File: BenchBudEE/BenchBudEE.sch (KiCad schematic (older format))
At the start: 0 parts

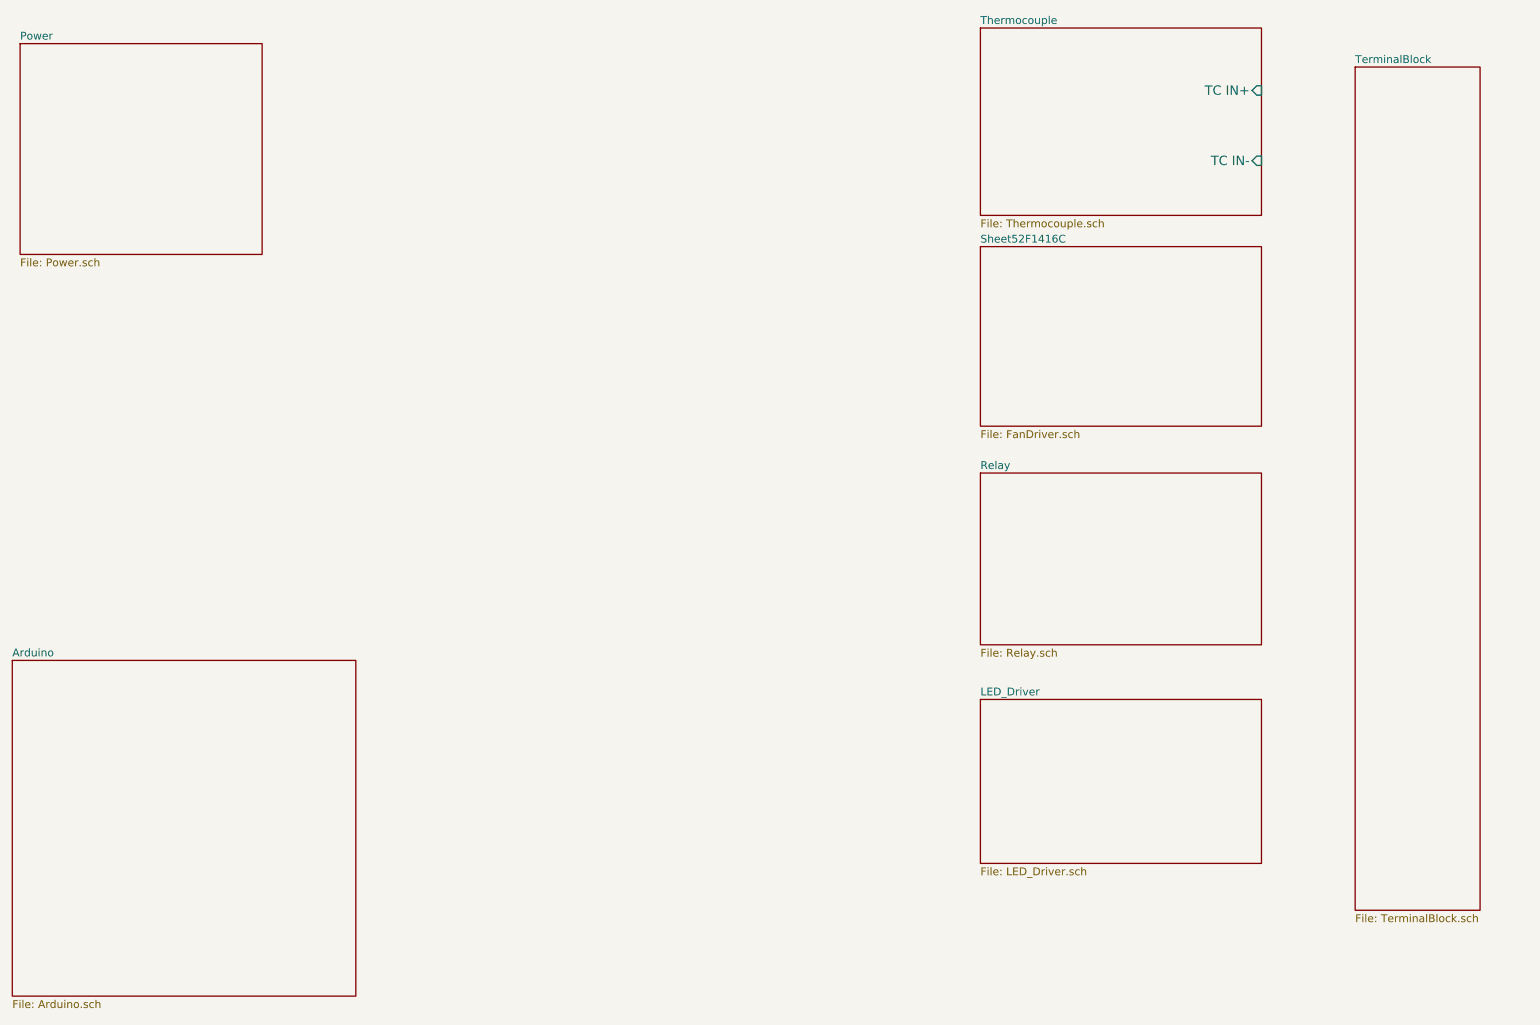
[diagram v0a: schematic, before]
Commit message: Added initial module I/O
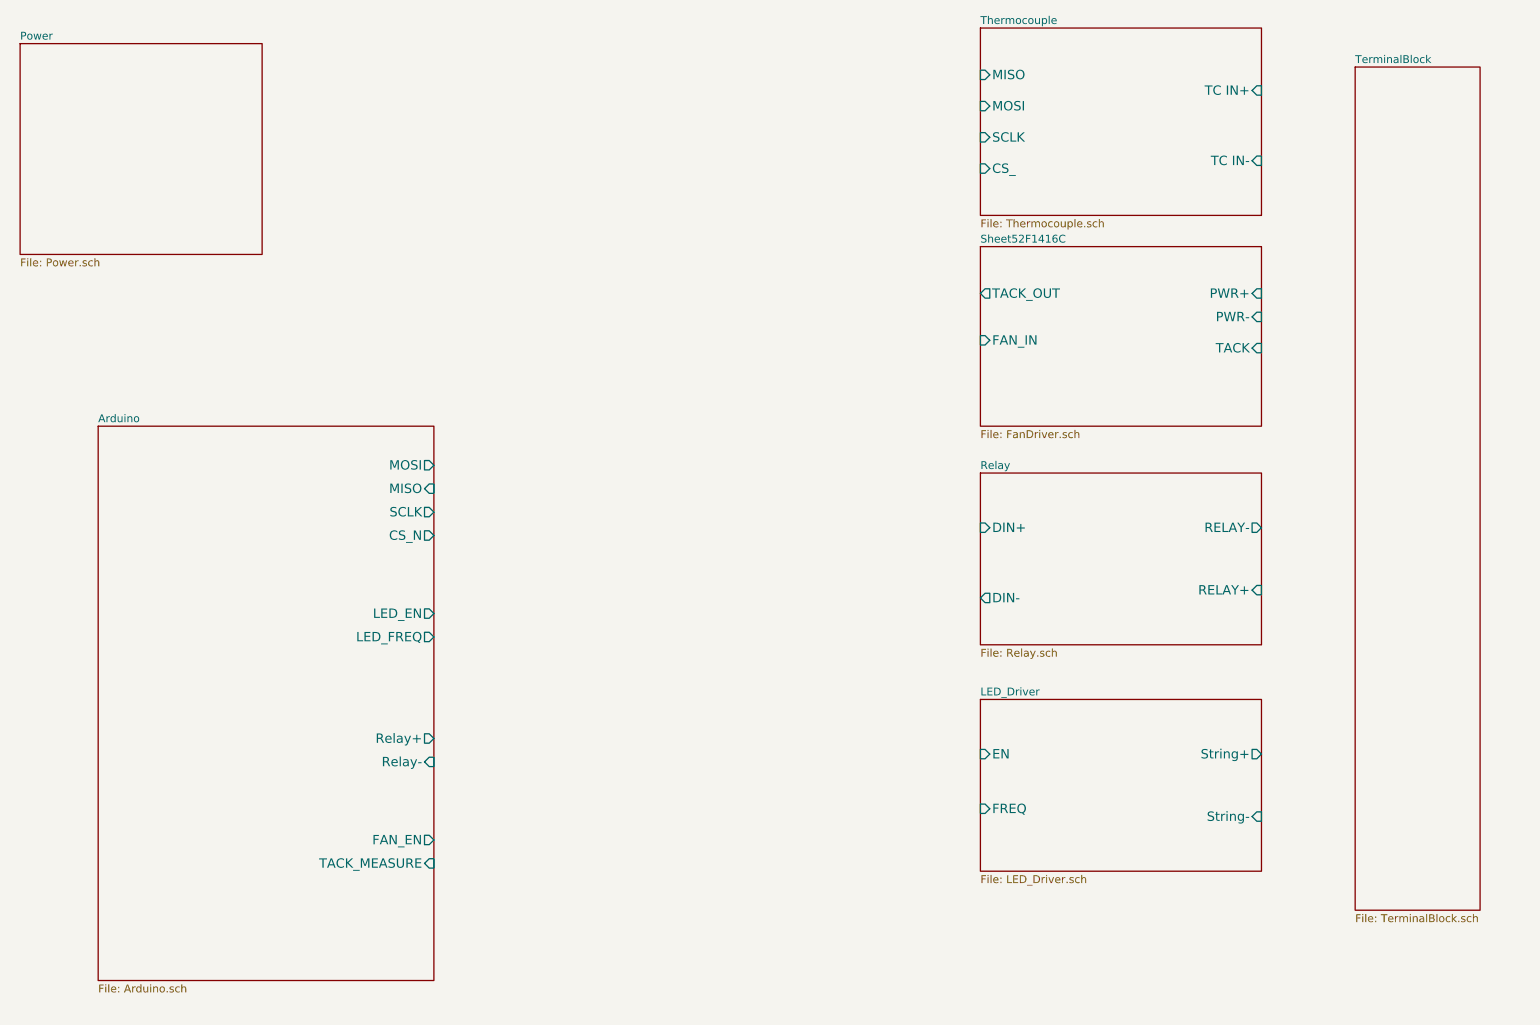
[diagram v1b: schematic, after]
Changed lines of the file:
@@
 F2 "TC IN+" I R 9200 1450 60
 F3 "TC IN-" I R 9200 1900 60
+F4 "MISO" I L 7400 1350 60
+F5 "MOSI" I L 7400 1550 60
+F6 "SCLK" I L 7400 1750 60
+F7 "CS_" I L 7400 1950 60
 $EndSheet
 $Sheet
@@
 F0 "Sheet52F1416C" 50
 F1 "FanDriver.sch" 50
+F2 "PWR+" I R 9200 2750 60
+F3 "PWR-" I R 9200 2900 60
+F4 "TACK" I R 9200 3100 60
+F5 "TACK_OUT" O L 7400 2750 60
+F6 "FAN_IN" I L 7400 3050 60
 $EndSheet
 $Sheet
-S 1200 5100 2200 2150
+S 1750 3600 2150 3550
 U 52F141E3
 F0 "Arduino" 50
 F1 "Arduino.sch" 50
+F2 "MOSI" O R 3900 3850 60
+F3 "MISO" I R 3900 4000 60
+F4 "SCLK" O R 3900 4150 60
+F5 "CS_N" O R 3900 4300 60
+F6 "Relay+" O R 3900 5600 60
+F7 "Relay-" I R 3900 5750 60
+F8 "LED_EN" O R 3900 4800 60
+F9 "LED_FREQ" O R 3900 4950 60
+F10 "FAN_EN" O R 3900 6250 60
+F11 "TACK_MEASURE" I R 3900 6400 60
 $EndSheet
 $Sheet
@@
 F0 "Relay" 50
 F1 "Relay.sch" 50
+F2 "DIN+" I L 7400 4250 60
+F3 "DIN-" O L 7400 4700 60
+F4 "RELAY-" O R 9200 4250 60
+F5 "RELAY+" I R 9200 4650 60
 $EndSheet
 $Sheet
-S 7400 5350 1800 1050
+S 7400 5350 1800 1100
 U 52F14293
 F0 "LED_Driver" 50
 F1 "LED_Driver.sch" 50
+F2 "EN" I L 7400 5700 60
+F3 "FREQ" I L 7400 6050 60
+F4 "String+" O R 9200 5700 60
+F5 "String-" I R 9200 6100 60
 $EndSheet
 $Sheet

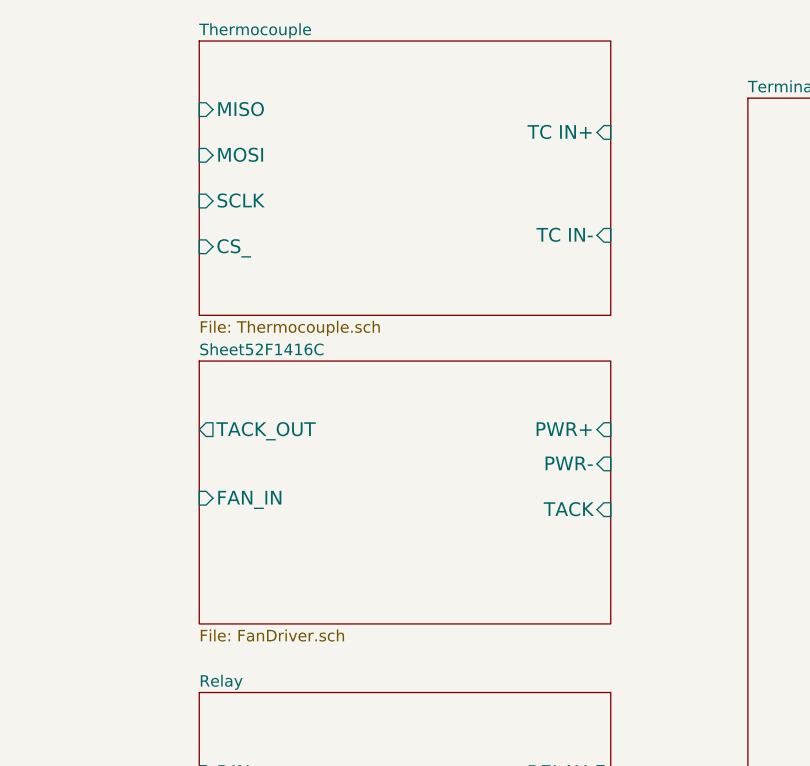
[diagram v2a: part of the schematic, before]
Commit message: Created Fan Module block diagram + added new I/O + minor spelling corrections
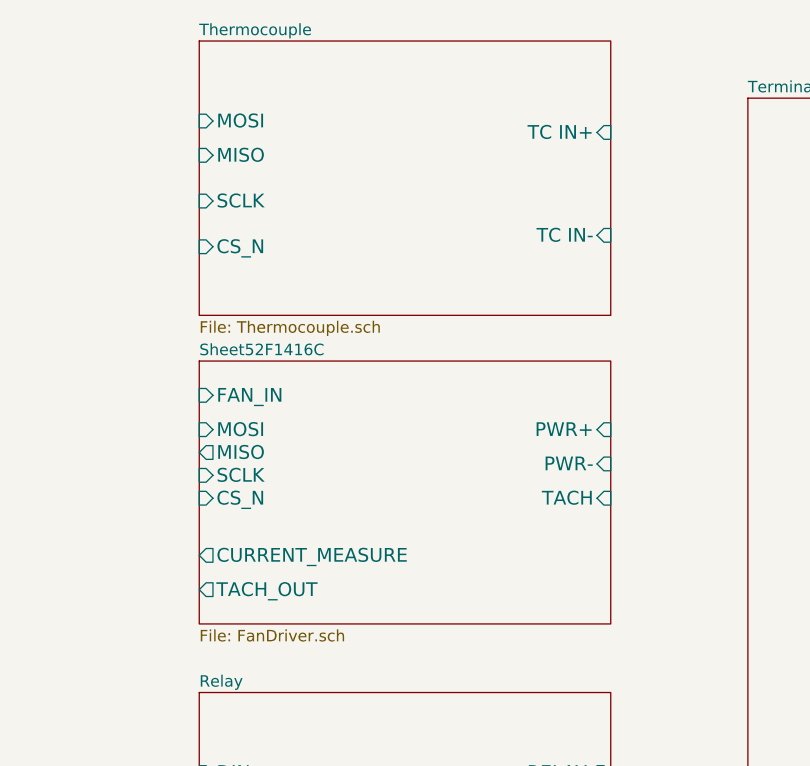
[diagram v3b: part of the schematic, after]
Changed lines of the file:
@@
 $EndDescr
-$Sheet
-S 7400 1050 1800 1200
-U 52F14139
-F0 "Thermocouple" 50
-F1 "Thermocouple.sch" 50
-F2 "TC IN+" I R 9200 1450 60
-F3 "TC IN-" I R 9200 1900 60
-F4 "MISO" I L 7400 1350 60
-F5 "MOSI" I L 7400 1550 60
-F6 "SCLK" I L 7400 1750 60
-F7 "CS_" I L 7400 1950 60
-$EndSheet
-$Sheet
-S 7400 2450 1800 1150
-U 52F1416D
-F0 "Sheet52F1416C" 50
-F1 "FanDriver.sch" 50
-F2 "PWR+" I R 9200 2750 60
-F3 "PWR-" I R 9200 2900 60
-F4 "TACK" I R 9200 3100 60
-F5 "TACK_OUT" O L 7400 2750 60
-F6 "FAN_IN" I L 7400 3050 60
-$EndSheet
 $Sheet
 S 1750 3600 2150 3550
@@
 F1 "Power.sch" 50
 $EndSheet
+$Sheet
+S 7400 2450 1800 1150
+U 52F1416D
+F0 "Sheet52F1416C" 50
+F1 "FanDriver.sch" 50
+F2 "PWR+" I R 9200 2750 60
+F3 "PWR-" I R 9200 2900 60
+F4 "FAN_IN" I L 7400 2600 60
+F5 "TACH" I R 9200 3050 60
+F6 "TACH_OUT" O L 7400 3450 60
+F7 "CURRENT_MEASURE" O L 7400 3300 60
+F8 "MOSI" I L 7400 2750 60
+F9 "MISO" O L 7400 2850 60
+F10 "SCLK" I L 7400 2950 60
+F11 "CS_N" I L 7400 3050 60
+$EndSheet
+$Sheet
+S 7400 1050 1800 1200
+U 52F14139
+F0 "Thermocouple" 50
+F1 "Thermocouple.sch" 50
+F2 "TC IN+" I R 9200 1450 60
+F3 "TC IN-" I R 9200 1900 60
+F4 "MISO" I L 7400 1550 60
+F5 "MOSI" I L 7400 1400 60
+F6 "SCLK" I L 7400 1750 60
+F7 "CS_N" I L 7400 1950 60
+$EndSheet
 $EndSCHEMATC
